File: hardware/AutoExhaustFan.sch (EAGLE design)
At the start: 6 parts

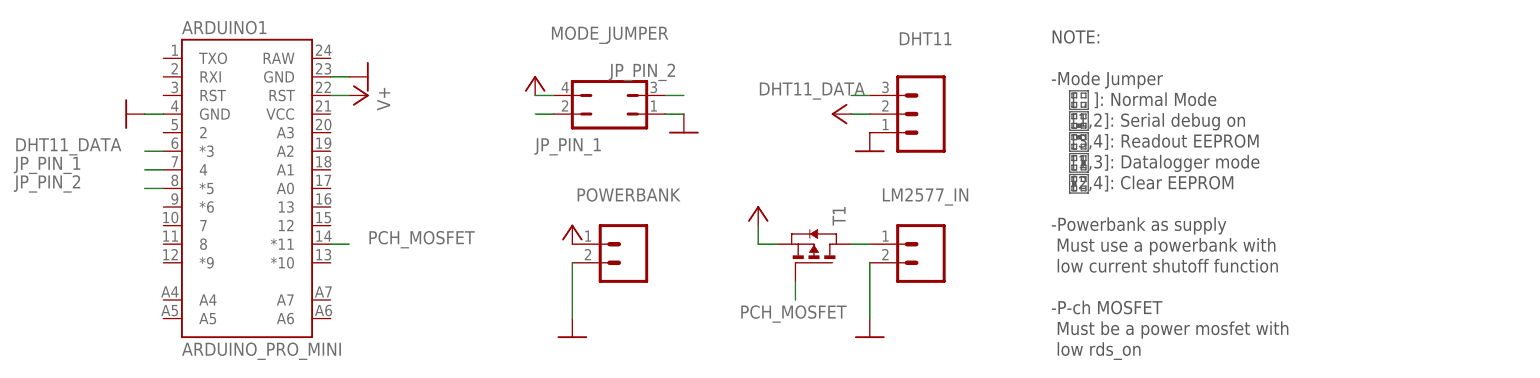
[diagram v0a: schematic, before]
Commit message: add decoupling capacitors
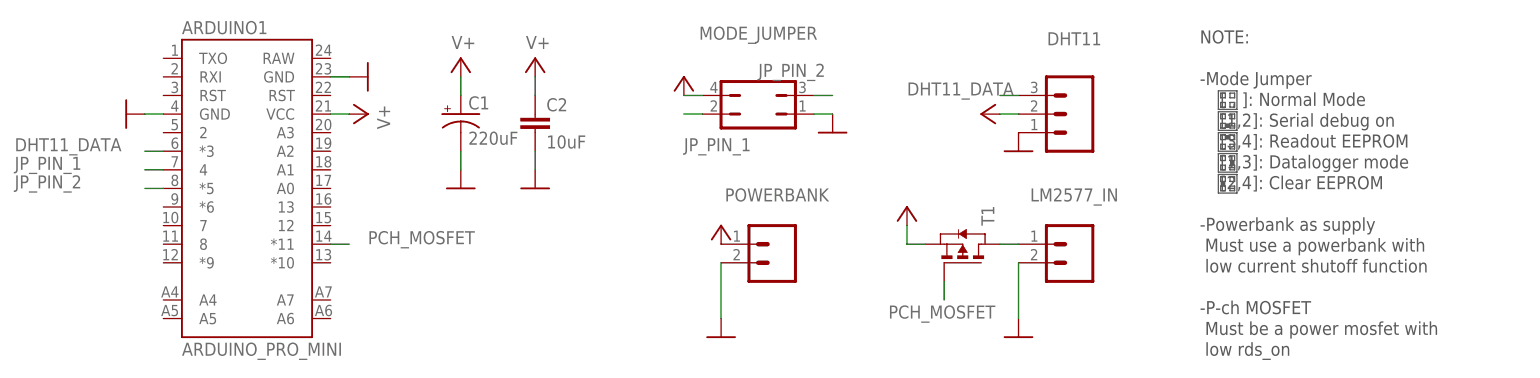
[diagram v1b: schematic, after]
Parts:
- added C1: 220uF, SparkFun-Capacitors:CAP_POLPTH1
- added C2: 10uF, SparkFun-Capacitors:CAP1206
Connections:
- net GND: now also C1.-, C2.2
- net V+: now also ARDUINO1.VCC, C1.+, C2.1; no longer ARDUINO1.RST@2
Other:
- moved on the sheet: DHT11, LM2577_IN, MODE_JUMPER, POWERBANK, T1
